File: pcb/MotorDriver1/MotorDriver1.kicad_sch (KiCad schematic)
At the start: 3 parts

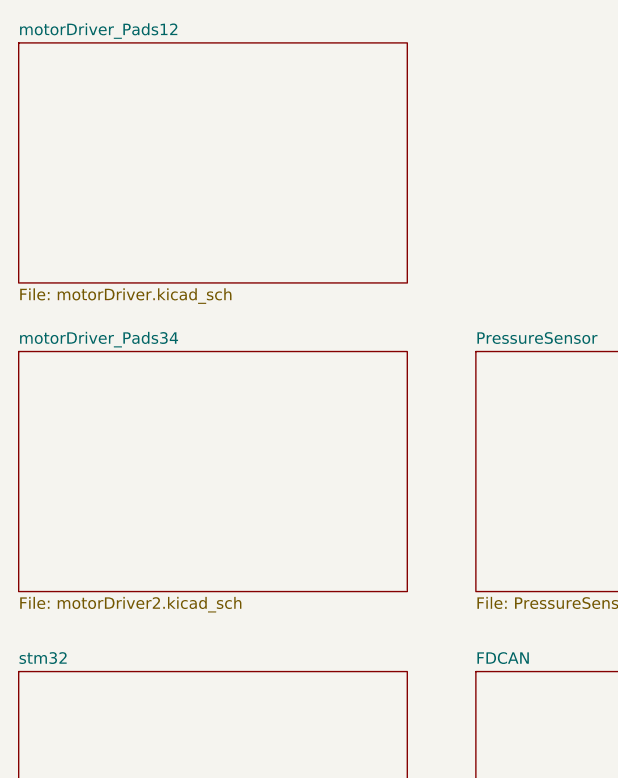
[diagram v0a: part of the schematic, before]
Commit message: Re-organized pcb files
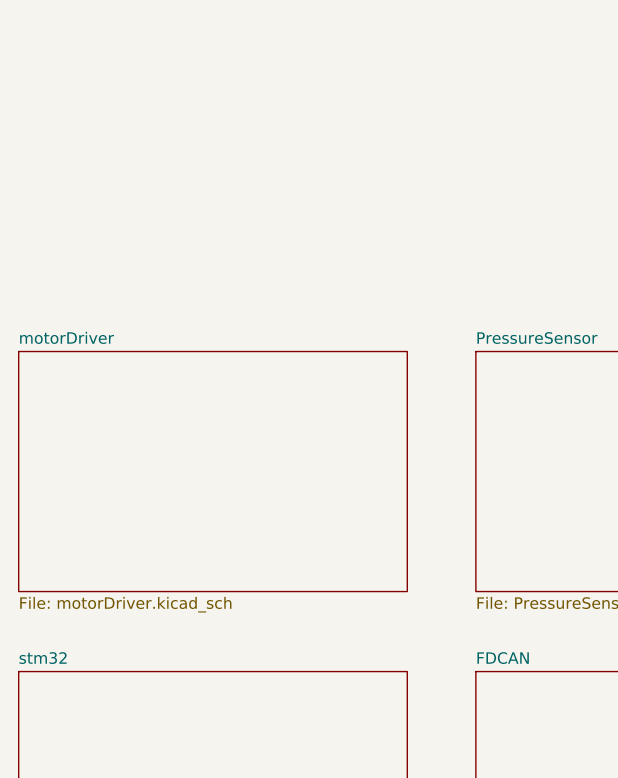
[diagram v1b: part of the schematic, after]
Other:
- sheet motorDriver_Pads12 renamed motorDriver
- removed sheet motorDriver_Pads34
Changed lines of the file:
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@@
-	)
-	(sheet
-		(at 26.67 119.38)
-		(size 43.18 26.67)
-		(exclude_from_sim no)
-		(in_bom yes)
-		(on_board yes)
-		(dnp no)
-		(fields_autoplaced yes)
-		(stroke
-			(width 0.1524)
-			(type solid)
-		)
-		(fill
-			(color 0 0 0 0.0000)
-		)
-		(property "Sheetname" "motorDriver_Pads34"
-			(at 26.67 118.6684 0)
-			(effects
-				(font
-					(size 1.27 1.27)
-				)
-				(justify left bottom)
-			)
-		)
-		(property "Sheetfile" "motorDriver2.kicad_sch"
-			(at 26.67 146.6346 0)
-			(effects
-				(font
-					(size 1.27 1.27)
-				)
-				(justify left top)
-			)
-		)
-		(instances
-			(project "MotorDriver1"
-				(path "/79cc9cfe-04d6-4d00-aa84-feae66cf8c45"
-					(page "6")
-				)
-			)
-		)
 	)
 	(sheet
@@
 	)
 	(sheet
-		(at 26.67 85.09)
+		(at 26.67 119.38)
 		(size 43.18 26.67)
 		(exclude_from_sim no)
@@
 		(on_board yes)
 		(dnp no)
+		(fields_autoplaced yes)
 		(stroke
 			(width 0.1524)
@@
 			(color 0 0 0 0.0000)
 		)
-		(property "Sheetname" "motorDriver_Pads12"
-			(at 26.67 84.3784 0)
+		(property "Sheetname" "motorDriver"
+			(at 26.67 118.6684 0)
 			(effects
 				(font
@@
 		)
 		(property "Sheetfile" "motorDriver.kicad_sch"
-			(at 26.67 112.3446 0)
+			(at 26.67 146.6346 0)
 			(effects
 				(font
